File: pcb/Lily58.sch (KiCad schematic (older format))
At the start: 119 parts, among them J1 LED, J2 4PIN, P1 i2c_pin, P2 i2c_pin, P3 ICSP, P4 OLED, SW1 SW_PUSH, SW10 SW_PUSH, SW11 SW_PUSH, SW12 SW_PUSH, SW13 SW_PUSH, SW14 SW_PUSH, SW15 SW_PUSH, SW16 SW_PUSH, SW17 SW_PUSH, SW18 SW_PUSH, SW19 SW_PUSH, SW2 SW_PUSH, SW20 SW_PUSH, SW21 SW_PUSH, SW22 SW_PUSH, SW23 SW_PUSH, SW24 SW_PUSH, SW25 SW_PUSH, SW26 SW_PUSH, SW27 SW_PUSH, SW28 SW_PUSH, SW29 SW_PUSH, SW3 SW_PUSH, SW4 SW_PUSH, SW5 SW_PUSH, SW6 SW_PUSH, SW7 SW_PUSH, SW8 SW_PUSH, SW9 SW_PUSH, U1 ProMicro

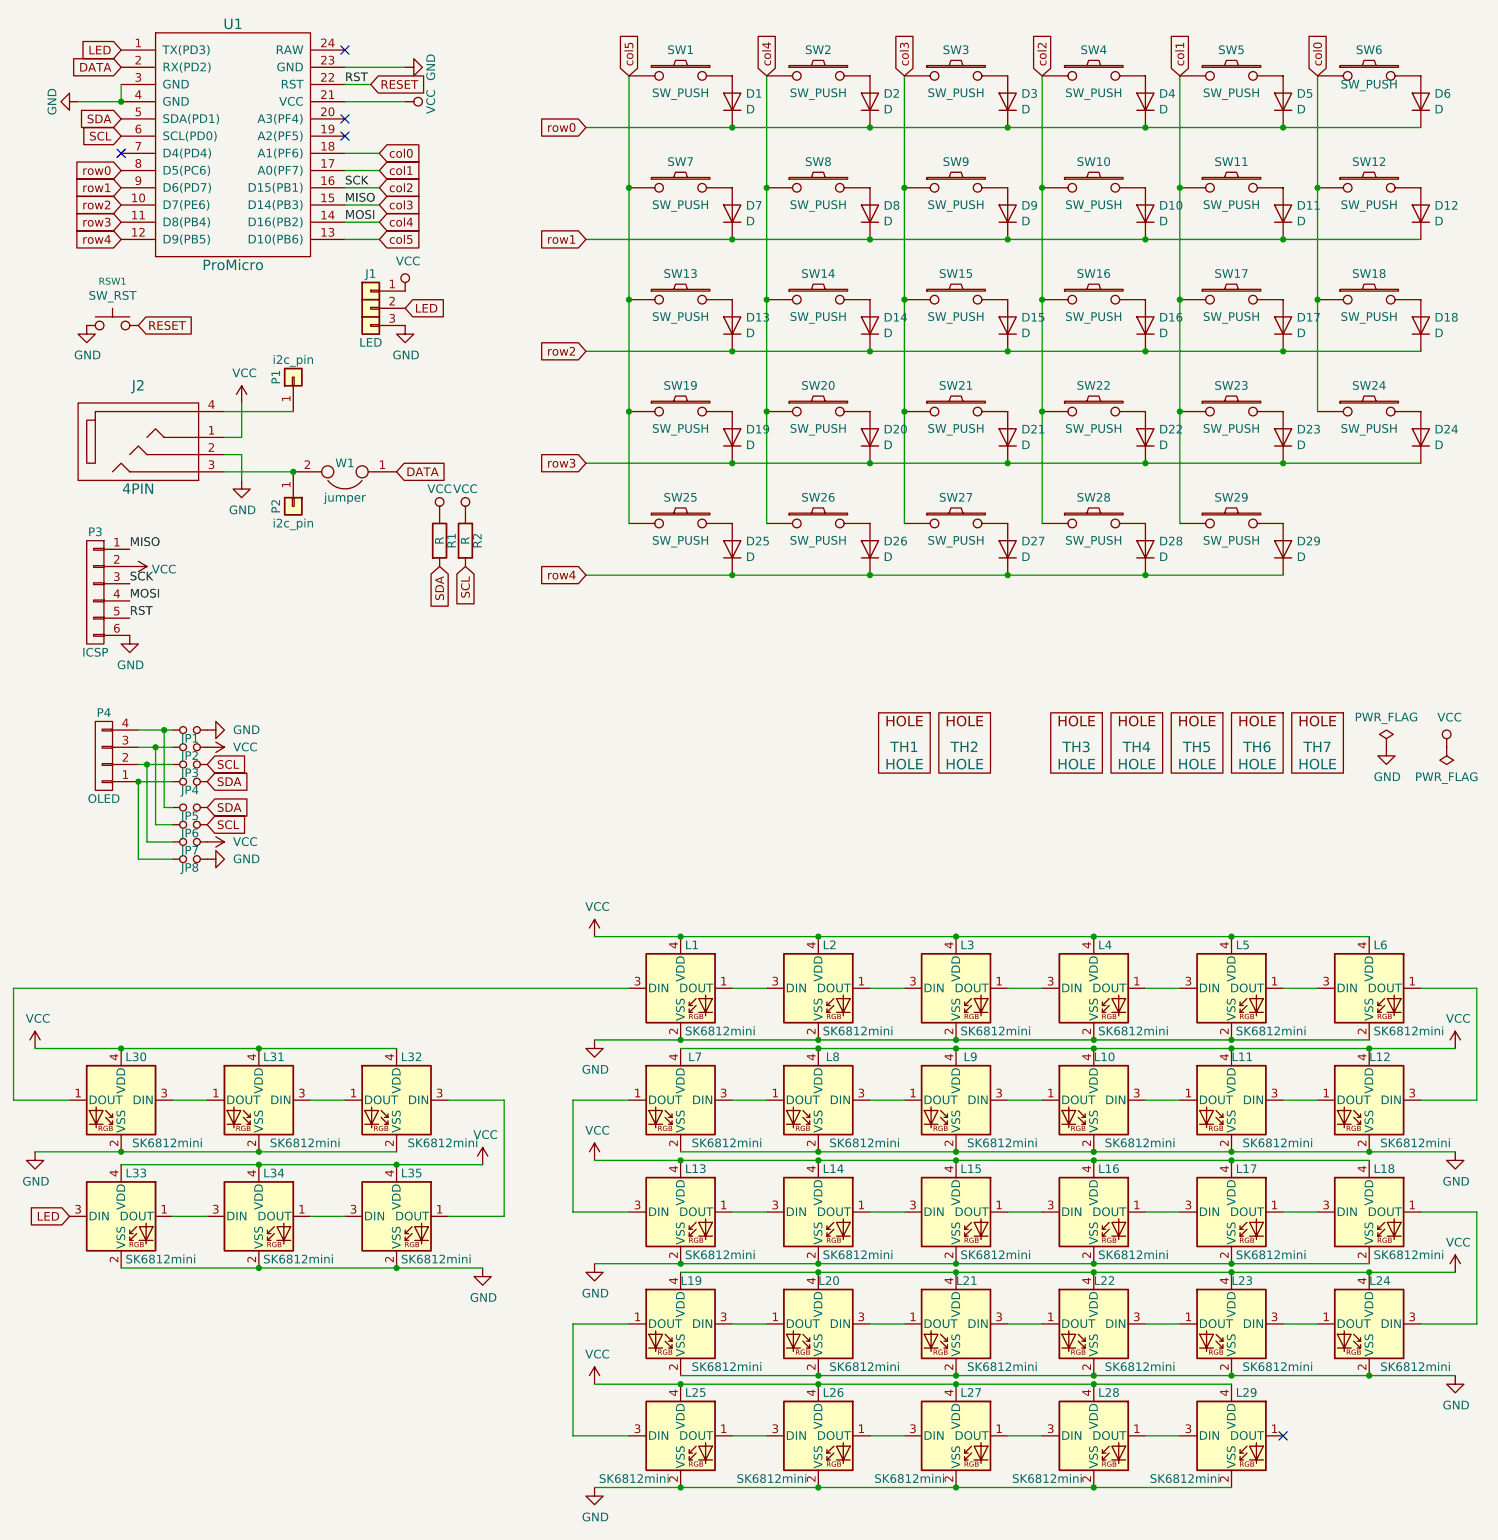
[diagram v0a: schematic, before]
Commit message: Added Encoder and 1 led
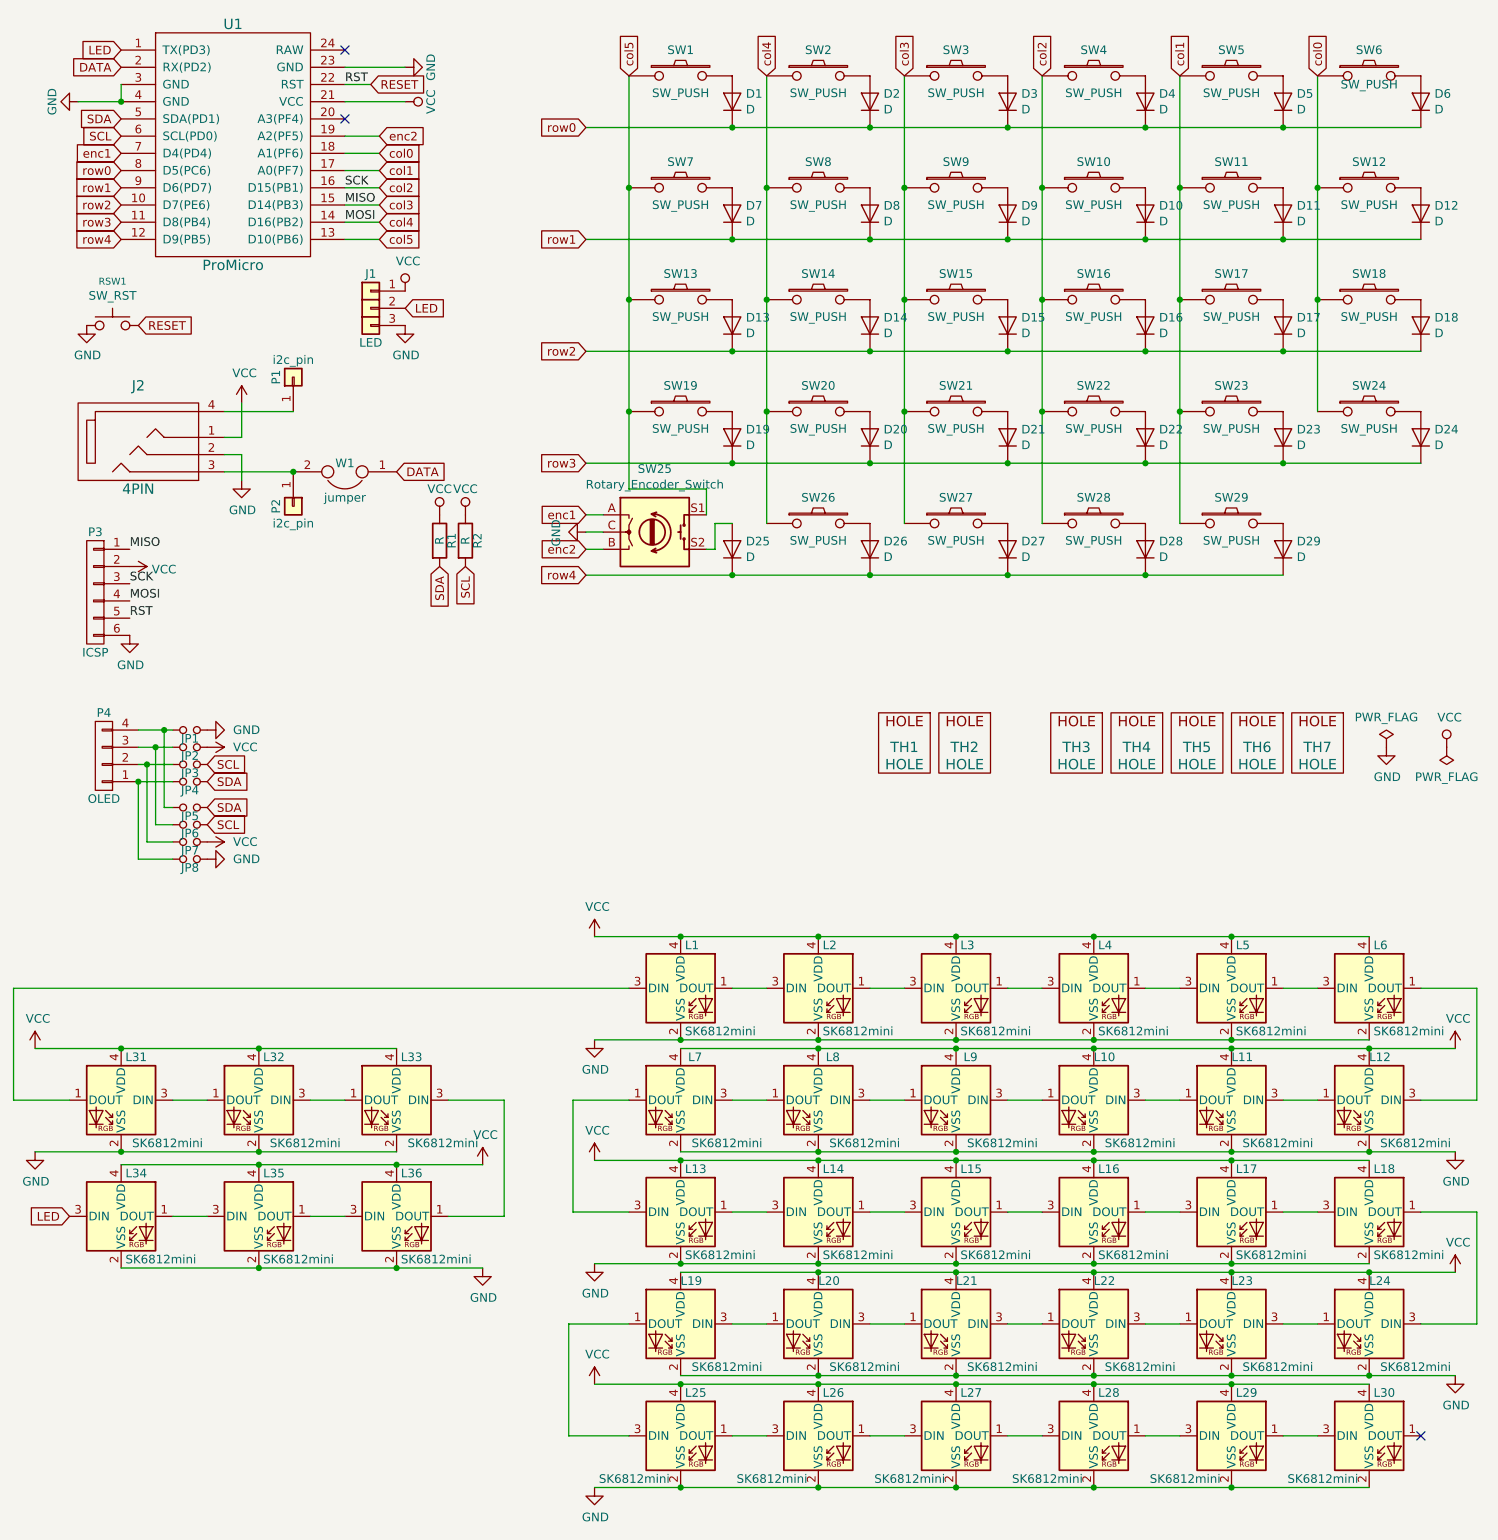
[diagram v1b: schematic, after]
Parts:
- removed SW25: SW_PUSH, Lily58-footprint:MX_PG1350_FLIP_HOLES_18mm, symbol Lily58-rescue:SW_PUSH-Lily58-cache
- added L25: SK6812mini, Lily58-footprint:SK6812MINI_rev, symbol LED:SK6812MINI
- added SW25: Rotary_Encoder_Switch, Lily58-footprint:RotaryEncoder_Alps_EC11E-Switch_Vertical_H20mm, symbol Device:Rotary_Encoder_Switch
- renumbered L25 to L26, L26 to L27, L27 to L28, L28 to L29, L29 to L30, L30 to L31, L31 to L32, L32 to L33, L33 to L34, L34 to L35, L35 to L36
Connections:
- net GND: now also L25.2 (VSS), SW25.C
- net VCC: now also L25.4 (VDD)
- net col5: now also SW25.S1
- net enc2: now reaches U1.19 (A2(PF5))
- net enc2: now also SW25.B
- net enc1: now reaches U1.7 (D4(PD4))
- net enc1: now also SW25.A
- net at D25.2 (A): now also SW25.S2
- net at L19.1 (DOUT): now also L25.3 (DIN); no longer L26.3 (DIN)
- new net: L25.1 (DOUT), L26.3 (DIN)
- no-connect marks 5 -> 3
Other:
- moved on the sheet: L26, L27, L28, L29, L30
